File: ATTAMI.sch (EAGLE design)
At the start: 19 parts, among them J1 CON_HEADER_1X02-PTH, J2 MICRO-USB_ALIEXPRESS, J3 CON_HEADER_1X02-PTH, J4 CON_HEADER_1X06-PTH, U1 MIC5225, U2 ATTINY85

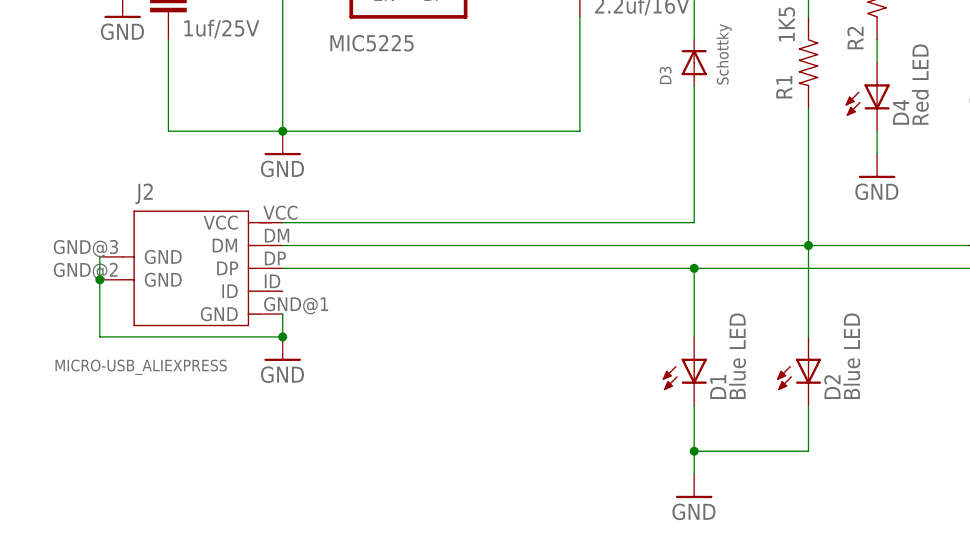
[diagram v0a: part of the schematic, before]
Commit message: ver 17
changed usb connector
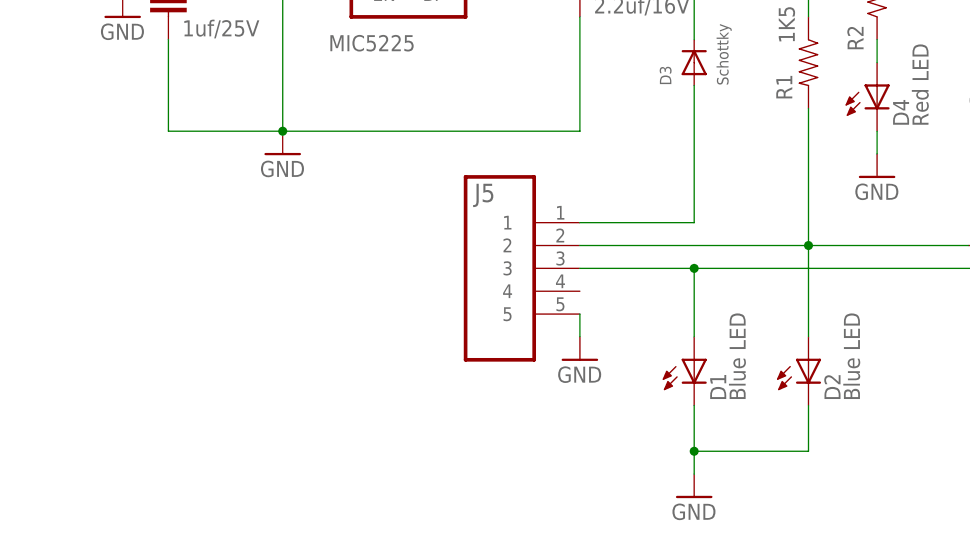
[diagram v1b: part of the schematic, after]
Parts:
- removed J2: MICRO-USB_ALIEXPRESS, yair_r:MICRO-USB_ALIEXPRESS
- added J5: (no value), Molex-47346-0001:47346-0001
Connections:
- removed net N$10: D2.A, J2.DM, R1.2, R3.1
- removed net N$7: D1.A, J2.DP, R4.1
- new net DM: D2.A, J5.2, R1.2, R3.1
- new net DP: D1.A, J5.3, R4.1
- net GND: now also J5.5; no longer J2.GND@1, J2.GND@2, J2.GND@3
- net V-BUS: now also J5.1; no longer J2.VCC
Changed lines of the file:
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@@
 <?xml version="1.0" encoding="utf-8"?>
 <!DOCTYPE eagle SYSTEM "eagle.dtd">
-<eagle version="6.3">
+<eagle version="6.5.0">
 <drawing>
 <settings>
@@
 <part name="U$1" library="microbuilder" deviceset="MOUNTINGHOLE" device="2.0" value="MOUNTINGHOLE2.0"/>
 <part name="S1" library="SparkFun-Electromechanical" deviceset="SWITCH-MOMENTARY-2" device="-SMD-1101NE"/>
-<part name="J2" library="yair_r" deviceset="MICRO-USB_ALIEXPRESS" device=""/>
 <part name="GND4" library="SparkFun" deviceset="GND" device=""/>
 <part name="U$2" library="microbuilder" deviceset="MOUNTINGHOLE" device="2.0" value="MOUNTINGHOLE2.0"/>
@@
 <part name="J4" library="dp_devices" deviceset="CON_HEADER_1X06" device="-PTH"/>
 <part name="FRAME1" library="frames" deviceset="A4L-LOC" device=""/>
+<part name="J5" library="Molex-47346-0001" deviceset="47346-0001" device=""/>
 </parts>
 <sheets>
@@
 <attribute name="NAME" x="187.96" y="124.46" size="1.778" layer="95" rot="R90"/>
 </instance>
-<instance part="J2" gate="G$1" x="48.26" y="104.14" smashed="yes">
-<attribute name="NAME" x="42.164" y="111.76" size="1.778" layer="95" ratio="10"/>
-<attribute name="VALUE" x="33.02" y="92.71" size="1.27" layer="95" ratio="10"/>
-</instance>
-<instance part="GND4" gate="1" x="58.42" y="93.98"/>
+<instance part="GND4" gate="1" x="91.44" y="93.98"/>
 <instance part="U$2" gate="G$1" x="142.24" y="162.56"/>
 <instance part="J1" gate="J" x="33.02" y="144.78" rot="MR0"/>
@@
 <instance part="J4" gate="G$1" x="215.9" y="139.7"/>
 <instance part="FRAME1" gate="G$1" x="0" y="0"/>
+<instance part="J5" gate="G$1" x="81.28" y="104.14" smashed="yes" rot="MR0">
+<attribute name="NAME" x="82.042" y="111.506" size="2.032" layer="95" ratio="10" rot="MR0"/>
+<attribute name="VALUE" x="86.36" y="88.9" size="2.0828" layer="96" ratio="10" rot="MR0"/>
+</instance>
 </instances>
 <busses>
 </busses>
 <nets>
-<net name="N$10" class="0">
+<net name="DM" class="0">
 <segment>
 <pinref part="R3" gate="G$1" pin="1"/>
@@
 <wire x1="116.84" y1="96.52" x2="116.84" y2="106.68" width="0.1524" layer="91"/>
 <pinref part="D2" gate="LED" pin="A"/>
-<pinref part="J2" gate="G$1" pin="DM"/>
-<wire x1="116.84" y1="106.68" x2="58.42" y2="106.68" width="0.1524" layer="91"/>
+<wire x1="116.84" y1="106.68" x2="91.44" y2="106.68" width="0.1524" layer="91"/>
+<pinref part="J5" gate="G$1" pin="2"/>
 </segment>
 </net>
@@
 </segment>
 <segment>
-<pinref part="J2" gate="G$1" pin="GND@1"/>
 <pinref part="GND4" gate="1" pin="GND"/>
-<wire x1="58.42" y1="99.06" x2="58.42" y2="96.52" width="0.1524" layer="91"/>
-<pinref part="J2" gate="G$1" pin="GND@2"/>
-<pinref part="J2" gate="G$1" pin="GND@3"/>
-<wire x1="38.1" y1="102.87" x2="38.1" y2="105.41" width="0.1524" layer="91"/>
-<wire x1="38.1" y1="102.87" x2="38.1" y2="96.52" width="0.1524" layer="91"/>
-<wire x1="38.1" y1="96.52" x2="58.42" y2="96.52" width="0.1524" layer="91"/>
-<junction x="38.1" y="102.87"/>
-<junction x="58.42" y="96.52"/>
+<wire x1="91.44" y1="99.06" x2="91.44" y2="96.52" width="0.1524" layer="91"/>
+<pinref part="J5" gate="G$1" pin="5"/>
 </segment>
 </net>
@@
 </segment>
 </net>
-<net name="N$7" class="0">
+<net name="DP" class="0">
 <segment>
 <pinref part="R4" gate="G$1" pin="1"/>
@@
 <junction x="104.14" y="104.14"/>
 <pinref part="D1" gate="LED" pin="A"/>
-<pinref part="J2" gate="G$1" pin="DP"/>
-<wire x1="58.42" y1="104.14" x2="104.14" y2="104.14" width="0.1524" layer="91"/>
+<wire x1="91.44" y1="104.14" x2="104.14" y2="104.14" width="0.1524" layer="91"/>
+<pinref part="J5" gate="G$1" pin="3"/>
 </segment>
 </net>
@@
 <net name="V-BUS" class="0">
 <segment>
-<pinref part="J2" gate="G$1" pin="VCC"/>
 <pinref part="D3" gate="G$1" pin="A"/>
-<wire x1="58.42" y1="109.22" x2="104.14" y2="109.22" width="0.1524" layer="91"/>
+<wire x1="91.44" y1="109.22" x2="104.14" y2="109.22" width="0.1524" layer="91"/>
 <wire x1="104.14" y1="109.22" x2="104.14" y2="124.46" width="0.1524" layer="91"/>
-</segment>
-</net>
+<pinref part="J5" gate="G$1" pin="1"/>
+</segment>
+</net>

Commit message: sent to FAB
geekcon edition, with coincell
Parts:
- removed J4: CON_HEADER_1X06-PTH, dp_devices:CON_HEADER_1X06-PTH
- removed J5: (no value), Molex-47346-0001:47346-0001
- added COIN_CELL, COIN_CELL_GND: (no value), adafruit:PINHD-1X1CB
- added D5: Schottky, microbuilder:DIODESOD-323
- added J2: (no value), microbuilder:HEADER-1X2ROUND
- added SJ1: (no value), microbuilder:SOLDERJUMPERCLOSED
- added USB: MICRO-USB_ALIEXPRESS, yair_r:MICRO-USB_ALIEXPRESS
- J1: value CON_HEADER_1X02-PTH -> (none); device dp_devices:CON_HEADER_1X02-PTH -> microbuilder:HEADER-1X7ROUND
- J3: value CON_HEADER_1X02-PTH -> (none); device dp_devices:CON_HEADER_1X02-PTH -> microbuilder:HEADER-1X2ROUND
- R2: value 560R -> 1K5
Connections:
- removed net DM: D2.A, J5.2, R1.2, R3.1
- removed net DP: D1.A, J5.3, R4.1
- new net N$10: D2.A, R1.2, R3.1, USB.DM
- new net N$13: D4.C, SJ1.2
- new net N$4: COIN_CELL.1, D5.A
- new net N$7: D1.A, R4.1, USB.DP
- net GND: now also COIN_CELL_GND.1, J1.1, J2.2, SJ1.1, USB.GND@1, USB.GND@2, USB.GND@3; no longer D4.C, J1.2, J5.5
- net N$1: now also J1.5; no longer J4.4
- net N$15: now also J1.3; no longer J4.2
- net N$3: now also J1.2; no longer J4.1
- net N$5: now also J1.4; no longer J4.3
- net N$6: now also J1.6; no longer J4.5
- net N$8: now also J1.7; no longer J4.6
- net V-BUS: now also USB.VCC; no longer J5.1
- net VCC: now also D5.C
- net V_BAT: now also J2.1; no longer J1.1
